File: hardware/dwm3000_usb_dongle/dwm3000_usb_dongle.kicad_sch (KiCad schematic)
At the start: 20 parts, among them J1 USB-4AM103AS, J2 3221-10-0300-00, U1 STM32F042F6P6, U2 XC6220B331MR-G

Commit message: Switch MCU from STM32F042F6P6 to STM32C071F8P6
Same TSSOP20 footprint, but a materially different pinout that required
re-wiring the schematic:

- USB_DM/USB_DP now land on native PA11/PA12 (pins 16/17) -- no
  SYSCFG_CFGR1.PA11_PA12_RMP remap needed like the F042 required.
- This package has no NRST pin at all (traded for one more GPIO), so J2's
  SWD nRESET (pin 10) is now no-connect and the NRST filter cap is removed.
  Debuggers reset via software (AIRCR.SYSRESETREQ) instead.
- No separate VDDA pin either -- single VDD/VSS supply, so one 100nF
  decoupling cap instead of two.
- Re-mapped SPI1/DWM3000 control/LED signals onto the new pin numbers,
  keeping the same net names throughout.

STM32C071 isn't in this KiCad 7.0.11 install's bundled symbol library (it
was added upstream after this KiCad release, in a newer generator format
7.0.11 can't parse), so extra_symbols/STM32C071F8Px.kicad_sym vendors the
real upstream symbol as the source of truth for the pin table, and
gen_sch.py reproduces those pins in the older KiCad-7-compatible syntax.

Regenerated the netlist, schematic PDF, and the placed-footprint PCB;
verified the netlist's 16 signal nets + no-connects match the new pinout.

Co-Authored-By: Claude Sonnet 5 <noreply@anthropic.com>
Claude-Session: https://claude.ai/code/session_0115nx7Q2HiGYnps6zk84N7F
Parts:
- removed C4, C5: 100nF, Capacitor_SMD:C_0603_1608Metric, symbol Device:C
- removed U1: STM32F042F6P6, Package_SO:TSSOP-20_4.4x6.5mm_P0.65mm, symbol MCU_ST_STM32F0:STM32F042F6Px
- added U1: STM32C071F8P6, Package_SO:TSSOP-20_4.4x6.5mm_P0.65mm, symbol MCU_ST_STM32C0:STM32C071F8Px
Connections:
- net +3V3: now also U1.4 (VDD)
- net DWM_IRQ: now also U1.9 (PA2)
- net DWM_RSTN: now also U1.8 (PA1)
- net DWM_WAKEUP: now also U1.7 (PA0)
- net GND: now also U1.5 (VSS)
- net LED1_CTRL: now also U1.1 (PB7/PB8)
- net SPI_CS: now also U1.10 (PA3)
- net SPI_MISO: now also U1.13 (PA6)
- net SPI_MOSI: now also U1.14 (PA7)
- net SPI_SCK: now also U1.12 (PA5)
- net SWCLK: now also U1.19 (PA14/PA15)
- net SWDIO: now also U1.18 (PA13)
- net USB_DM_MCU: now also U1.16 (PA11)
- net USB_DP_MCU: now also U1.17 (PA12)
- net NRST: no longer names the net of J2.10 (Pin_10)
- no-connect marks 14 -> 17
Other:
- note added: "STM32C071F8P6 (Host MCU)"
- note removed: "STM32F042F6P6 (Host MCU)"

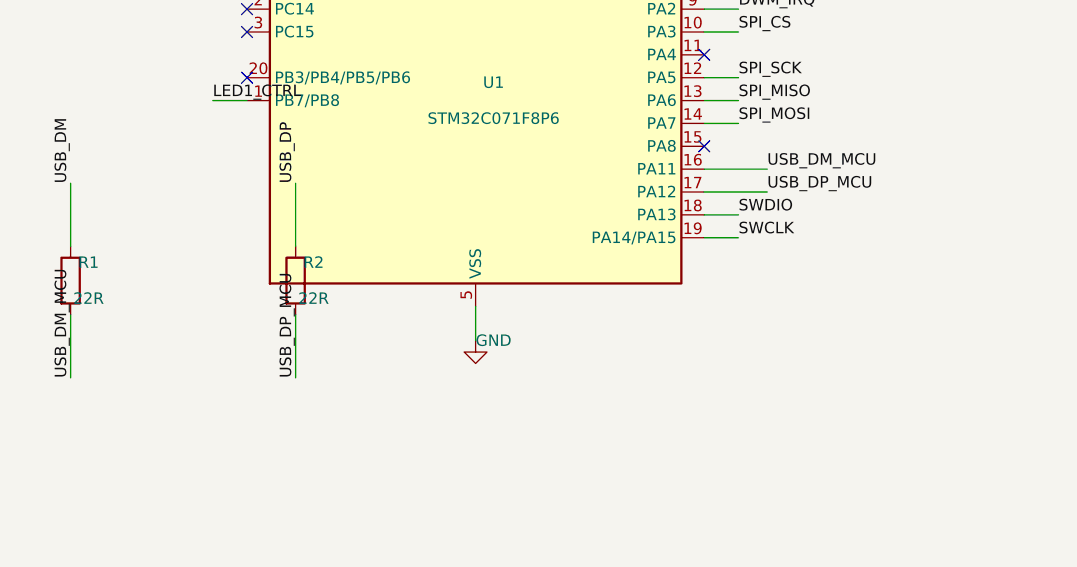
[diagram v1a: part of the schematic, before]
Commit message: Add DNP-by-default optional USB D+ pull-up (R6)
STM32C071's internal USB D+ pull-up almost certainly makes this
unnecessary -- every ST full-speed USB device peripheral in this IP
family (F0/G0/L0/C0) has had a software-controlled internal pull-up
(USB_BCDR.DPPU) -- but st.com wasn't reachable from here to confirm it
against the STM32C071 reference manual directly, so this adds a
footprint-only safety net instead of leaving it unresolved.

R6 (1.5k, USB_DP_MCU to +3V3, right at the R2/PA12 side) is placed on the
schematic and PCB with dnp=yes: it shows the standard DNP cross in the
schematic and is excluded from BOM/position files on the board, so normal
assembly doesn't populate it. Only stuff it if bring-up shows the device
isn't enumerating as full-speed.

Co-Authored-By: Claude Sonnet 5 <noreply@anthropic.com>
Claude-Session: https://claude.ai/code/session_0115nx7Q2HiGYnps6zk84N7F
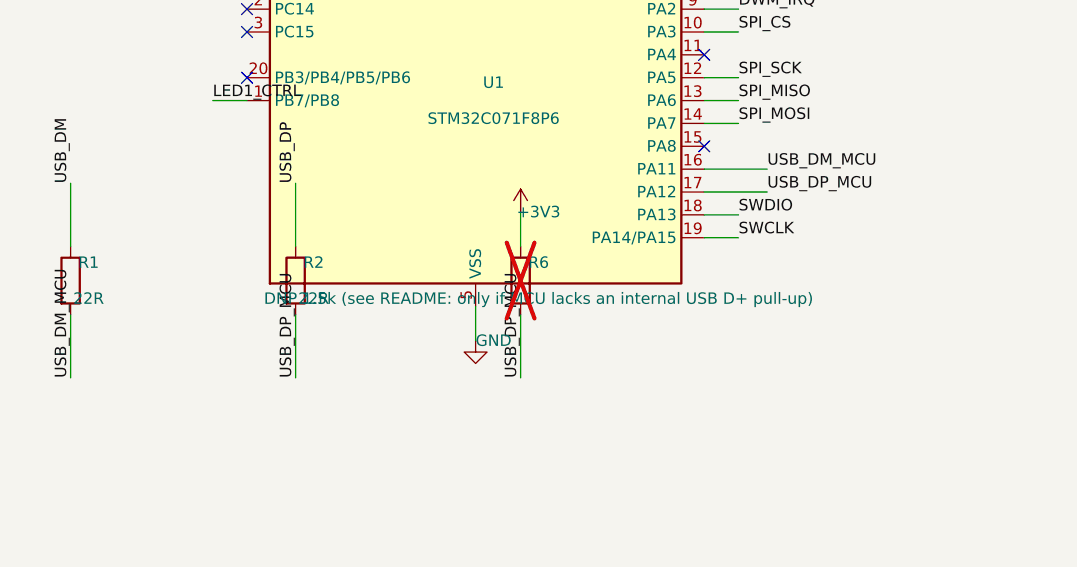
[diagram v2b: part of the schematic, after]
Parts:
- added R6: DNP 1.5k (see README: only if MCU lacks an intern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, Resistor_SMD:R_0603_1608Metric, symbol Device:R
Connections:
- net +3V3: now also R6.1
- net USB_DP_MCU: now also R6.2

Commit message: Fix: wire STM32 pin 6 (PF2-NRST) to SWD nRESET -- it is NOT a plain GPIO
A previous revision claimed the STM32C071F8Px TSSOP20 package "has no NRST
pin at all" and left both the MCU pin and J2's nRESET unconnected. That was
wrong. Pin 6 is named PF2-NRST in ST's own pin database (confirmed against
the public STM32_open_pin_data repo): it defaults to acting as a normal
reset input, and is only reassignable to plain PF2 GPIO via the
NRST_MODE[1:0] option byte (which this design does not set).

The KiCad symbol used to build extra_symbols/STM32C071F8Px.kicad_sym only
lists this pin's ordinary alternate functions (PF2/RCC_MCO/TIM1_CH4) since
the reset/GPIO duality is option-byte-controlled, not a normal AF, so it
never showed up in that pin table -- that's what led to the earlier mistake.

Fix: pin 6 is wired to J2 pin 10 (nRESET) like a normal NRST, with a 100nF
filter cap (C5) per ST's usual hardware design guidelines (AN2586). Hardware
connect-under-reset now works normally. README corrected with the real
mechanism and a pointer to ST's community-documented pitfalls of ever
reassigning this pin to GPIO mode.

Co-Authored-By: Claude Sonnet 5 <noreply@anthropic.com>
Claude-Session: https://claude.ai/code/session_0115nx7Q2HiGYnps6zk84N7F
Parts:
- added C5: 100nF, Capacitor_SMD:C_0603_1608Metric, symbol Device:C
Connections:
- net GND: now also C5.2
- net NRST: now reaches U1.6 (PF2)
- net NRST: now also J2.10 (Pin_10), C5.1
- no-connect marks 17 -> 15

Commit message: Add second MCU-driven status LED (D4/R7) on STM32 pin 20 (PB3)
Pin 20 is a 4-way multi-bonded pad (PB3/PB4/PB5/PB6 share one physical
pin) selected via the SYSCFG_CFGR3 register -- a normal peripheral
register, not a FLASH option byte like PF2-NRST/PA14-BOOT0, so there's no
unlock sequence or bricking risk: firmware just needs to select PB3 there
before configuring the pin as a GPIO output.

D4 (LED) + R7 (1k series resistor) added following the same +3V3->R->LED
anode->cathode->GPIO(sink) pattern as D1/R3, wired to a new LED2_CTRL net.
README updated (BOM, pin table, and a new explanatory note distinguishing
this ordinary multi-bond selection from the option-byte-special pins
documented earlier).

Co-Authored-By: Claude Sonnet 5 <noreply@anthropic.com>
Claude-Session: https://claude.ai/code/session_0115nx7Q2HiGYnps6zk84N7F
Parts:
- added D4: LED, LED_SMD:LED_0603_1608Metric, symbol Device:LED
- added R7: 1k, Resistor_SMD:R_0603_1608Metric, symbol Device:R
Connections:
- net +3V3: now also R7.1
- net LED2_CTRL: now reaches U1.20 (PB3/PB4/PB5/PB6)
- net LED2_CTRL: now also D4.1 (K)
- new net: D4.2 (A), R7.2
- no-connect marks 15 -> 14
